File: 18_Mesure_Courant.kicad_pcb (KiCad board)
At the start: 2 copper layers, 20.3 x 20.3 mm, 13 parts, among them J1 Conn_01x01, J2 Conn_01x01, J3 Conn_01x01, J4 Conn_01x01, J5 Conn_01x01, J6 Conn_01x01, J7 Conn_01x01, U1 ACS712xLCTR-20A

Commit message: maj split librairies
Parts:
- J1, J2, J3, J4, J5, J6, J7: footprint Chimere:Castellated_conn -> Chimere_mods:Castellated_conn

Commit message: maj kicad 6
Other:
- net class Default removed
- net class demi-gros removed
- net class gros removed

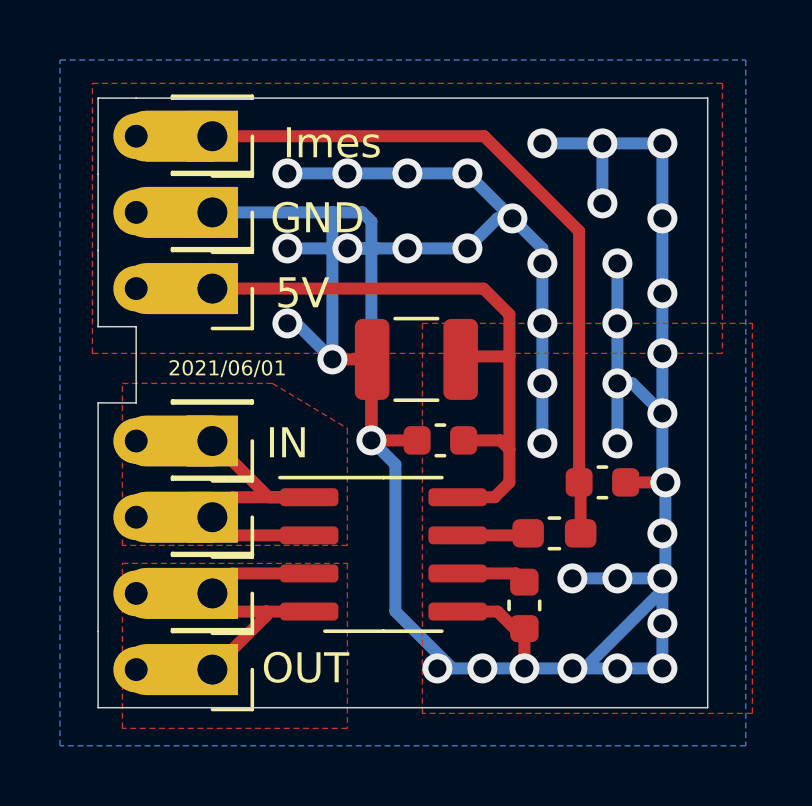
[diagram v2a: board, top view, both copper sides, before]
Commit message: maj pcb
maj liens librairies
maj empreinte
maj modèles 3D
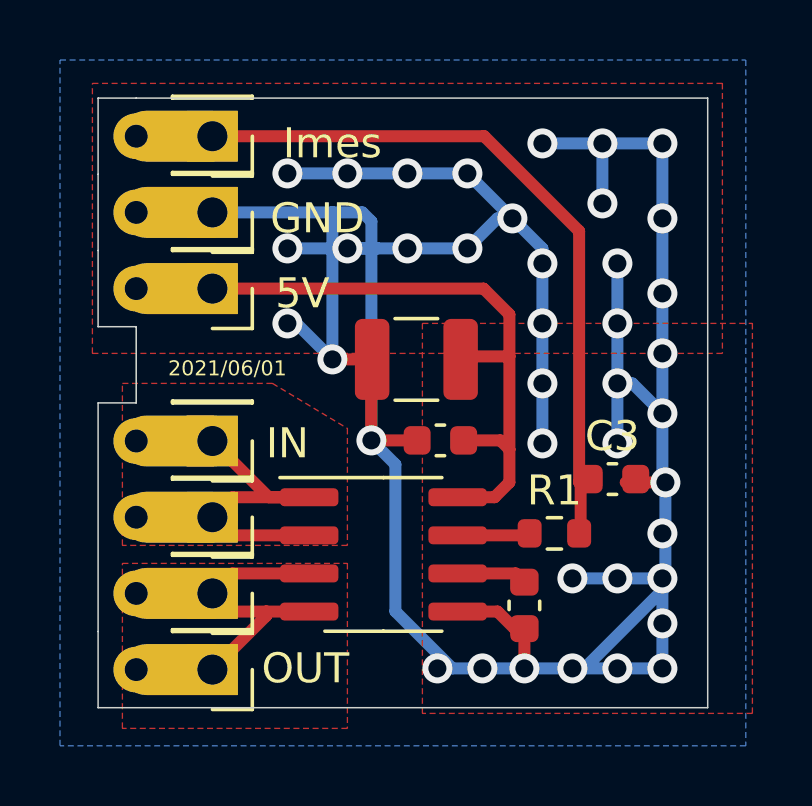
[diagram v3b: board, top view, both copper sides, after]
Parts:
- C1, C3: value 100nF -> 50V 100nF X7R ±10%
- C2: value 10uF -> 50V 10uF X7R ±10%
- C4: value 1nF -> 50V 1nF X7R ±10%
- R1: footprint Resistor_SMD:R_0603_1608Metric_Pad1.05x0.95mm_HandSolder -> Resistor_SMD:R_0603_1608Metric
- moved C3 0.35 mm to (117.5, 74.9)

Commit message: mise en place et routage
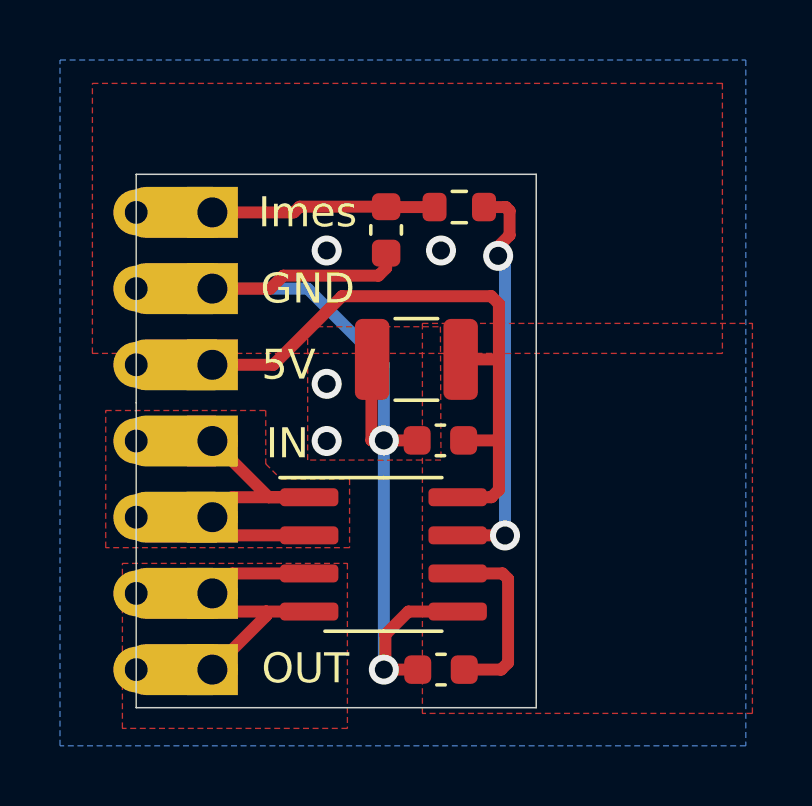
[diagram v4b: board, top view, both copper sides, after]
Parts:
- moved R1 11.3 mm to (112.4, 65.9), turned to 180 degrees
- moved C3 11.2 mm to (109.9, 66.6), turned to -90 degrees
- moved C4 3.51 mm to (111.8, 81.3), turned to 180 degrees
- moved J1 2.54 mm to (104.1, 66.0)
- moved J3 2.54 mm to (104.1, 71.1)
- moved J2 2.54 mm to (104.1, 68.6)
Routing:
- net GND: track 109.9 -> 32.7 mm, vias 40 -> 6
- net I_mes: track 23.6 -> 7.49 mm
- net Net-(R1-Pad1): track 2.38 -> 13.6 mm, vias 0 -> 2
- net Net-(C4-Pad1): track 2.35 -> 6.10 mm
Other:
- board size 20.3 x 20.3 mm -> 13.3 x 17.8 mm
- board text added: "18_Mesure_Courant"
- board text added: "2023/05/02"
- board text removed: "2021/06/01"
- board text removed: "github.com/ ThierryOrlandi/ 18_Mesure_Courant"

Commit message: maj config gerbers
génération des fichiers pour fabrication
ajout ref lcsc pour R1
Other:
- rule pad_to_mask_clearance: 0.05 -> 0
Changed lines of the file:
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@@
   )
   (setup
-    (pad_to_mask_clearance 0.05)
+    (stackup
+      (layer "F.SilkS" (type "Top Silk Screen"))
+      (layer "F.Paste" (type "Top Solder Paste"))
+      (layer "F.Mask" (type "Top Solder Mask") (thickness 0.01))
+      (layer "F.Cu" (type "copper") (thickness 0.035))
+      (layer "dielectric 1" (type "core") (thickness 1.51) (material "FR4") (epsilon_r 4.5) (loss_tangent 0.02))
+      (layer "B.Cu" (type "copper") (thickness 0.035))
+      (layer "B.Mask" (type "Bottom Solder Mask") (thickness 0.01))
+      (layer "B.Paste" (type "Bottom Solder Paste"))
+      (layer "B.SilkS" (type "Bottom Silk Screen"))
+      (copper_finish "None")
+      (dielectric_constraints no)
+    )
+    (pad_to_mask_clearance 0)
     (grid_origin 104.14 78.74)
     (pcbplotparams
       (layerselection 0x00310fc_ffffffff)
       (disableapertmacros false)
-      (usegerberextensions false)
-      (usegerberattributes true)
-      (usegerberadvancedattributes true)
+      (usegerberextensions true)
+      (usegerberattributes false)
+      (usegerberadvancedattributes false)
       (creategerberjobfile false)
       (svguseinch false)
       (svgprecision 6)
-      (excludeedgelayer false)
+      (excludeedgelayer true)
       (plotframeref false)
       (viasonmask false)
       (mode 1)
-      (useauxorigin true)
+      (useauxorigin false)
       (hpglpennumber 1)
       (hpglpenspeed 20)
@@
       (psa4output false)
       (plotreference true)
-      (plotvalue true)
+      (plotvalue false)
       (plotinvisibletext false)
       (sketchpadsonfab false)
-      (subtractmaskfromsilk false)
+      (subtractmaskfromsilk true)
       (outputformat 1)
       (mirror false)
@@
     (fp_line (start 1.6 -1.25) (end 1.6 1.25) (layer "F.Fab") (width 0.1))
     (fp_line (start -1.6 1.25) (end -1.6 -1.25) (layer "F.Fab") (width 0.1))
-    (pad "1" smd roundrect (at -1.475 0 180) (size 1.15 2.7) (layers "F.Cu" "F.Paste" "F.Mask") (roundrect_rratio 0.217391)
+    (pad "1" smd roundrect (at -1.475 0 180) (size 1.15 2.7) (layers "F.Cu" "F.Paste" "F.Mask") (roundrect_rratio 0.2173913043)
       (net 2 "5V") (pintype "passive"))
-    (pad "2" smd roundrect (at 1.475 0 180) (size 1.15 2.7) (layers "F.Cu" "F.Paste" "F.Mask") (roundrect_rratio 0.217391)
+    (pad "2" smd roundrect (at 1.475 0 180) (size 1.15 2.7) (layers "F.Cu" "F.Paste" "F.Mask") (roundrect_rratio 0.2173913043)
       (net 1 "GND") (pintype "passive"))
     (model "${KICAD6_3DMODEL_DIR}/Capacitor_SMD.3dshapes/C_1210_3225Metric.wrl"
